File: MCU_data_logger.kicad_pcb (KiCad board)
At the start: 2 copper layers, 51.7 x 39.1 mm, 29 parts, among them J1 I2C, J2 GPIO, J3 SERIAL, J4 ICSP, U1 24LC1025, U2 24LC1025, U3 DS1337S_, U4 ATMEGA328P-AU, Y1 32.768MHz, Y2 16MHz

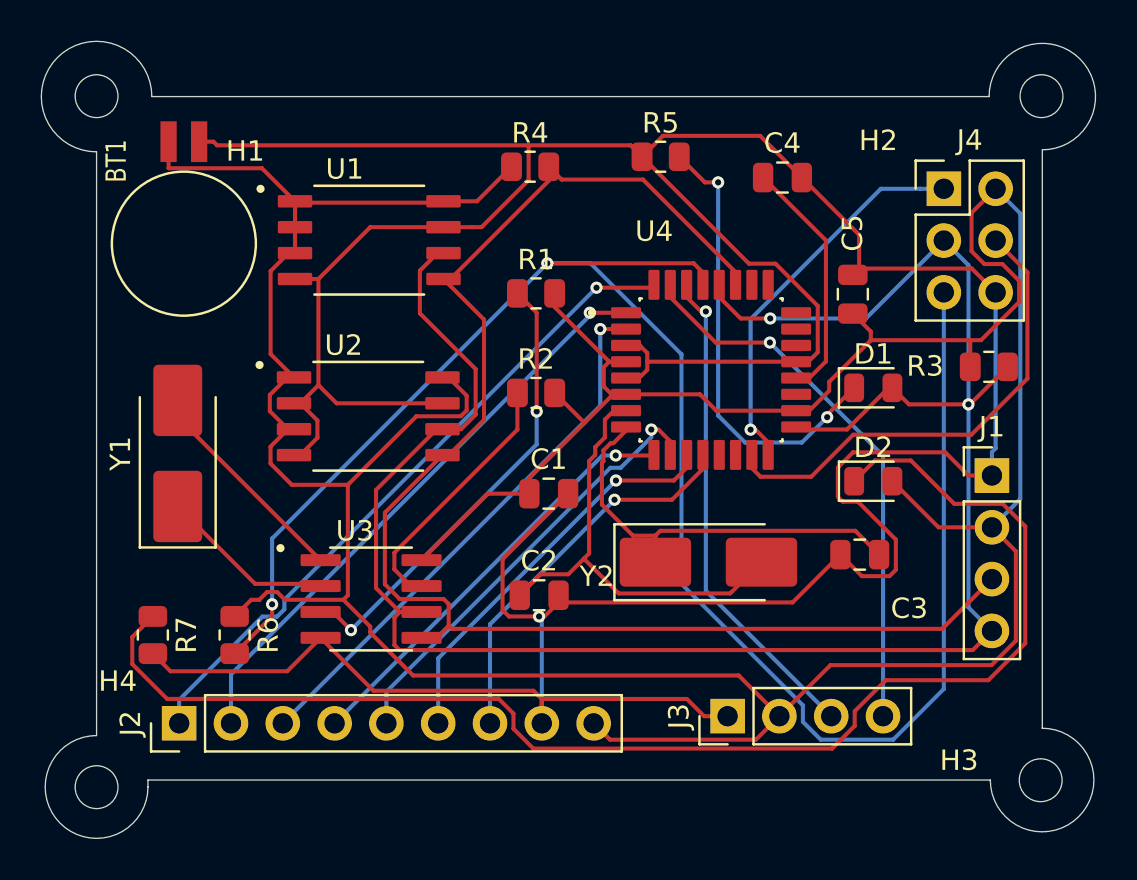
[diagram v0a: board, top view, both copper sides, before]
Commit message: Converted to 4 layer PCB
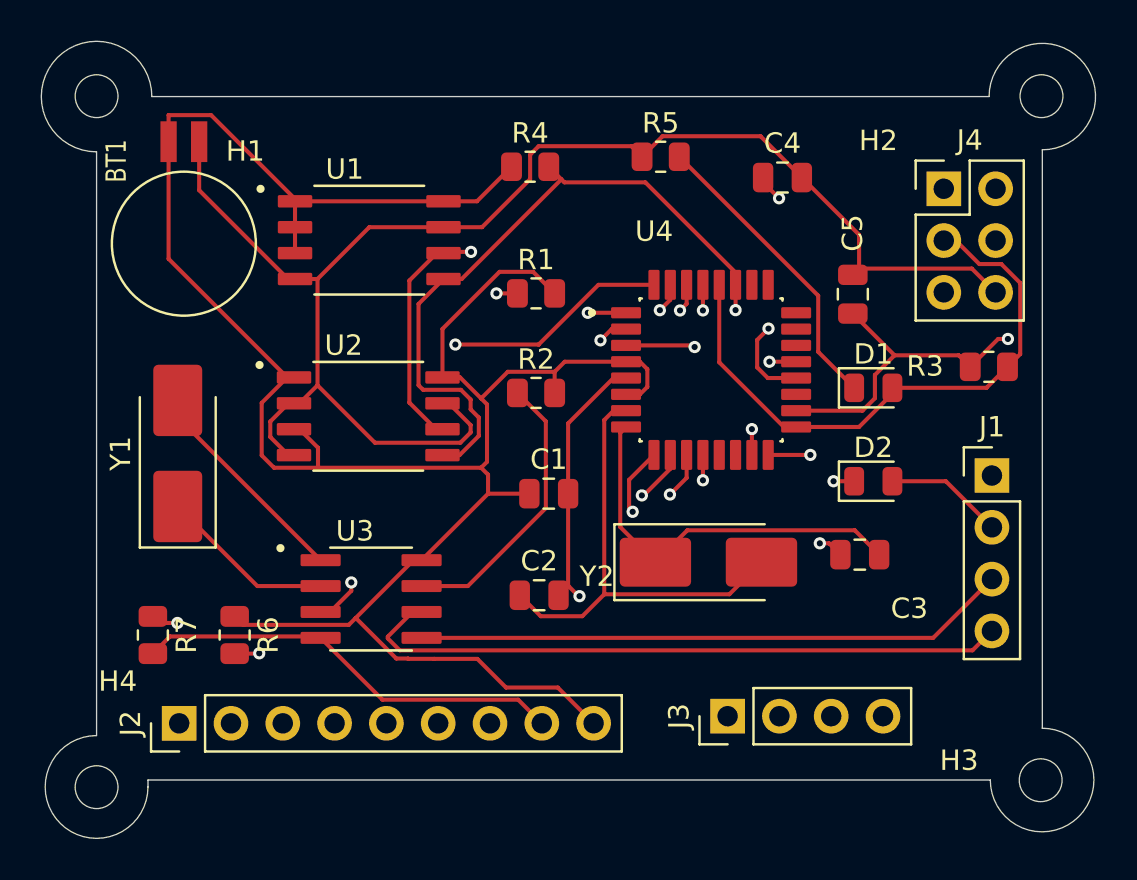
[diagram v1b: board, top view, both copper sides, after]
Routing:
- net /RESET: track 90.6 -> 44.0 mm
- net Net-(D2-K): track 67.1 -> 39.7 mm, vias 0 -> 2
- net /sda: track 71.4 -> 90.2 mm, vias 0 -> 1
- net GND: track 191.9 -> 173.8 mm, vias 1 -> 4
- net /sck: track 101.3 -> 117.4 mm, vias 2 -> 1
- net VCC: track 193.0 -> 179.3 mm, vias 0 -> 1
- net Net-(D1-K): track 22.3 -> 14.9 mm, vias 2 -> 0
- net /MOSI: track 23.7 -> 18.0 mm, vias 0 -> 1
- net /D2: track 33.1 -> 37.2 mm
- net /TX: track 27.0 -> 29.4 mm
- net /D6: track 21.9 -> 19.8 mm
- net Net-(U3-~{INTA}): track 22.5 -> 20.7 mm
- net /D8: track 19.1 -> 17.5 mm
- net /D7: track 19.9 -> 18.4 mm
- net /MISO: track 19.3 -> 18.0 mm
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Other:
- copper layers 2 -> 4
